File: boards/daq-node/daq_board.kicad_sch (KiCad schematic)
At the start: 14 parts, among them J1 917784-1, J11 Conn_01x19_Socket, J12 Conn_01x19_Socket, J4 917781-1, J7 917783-1

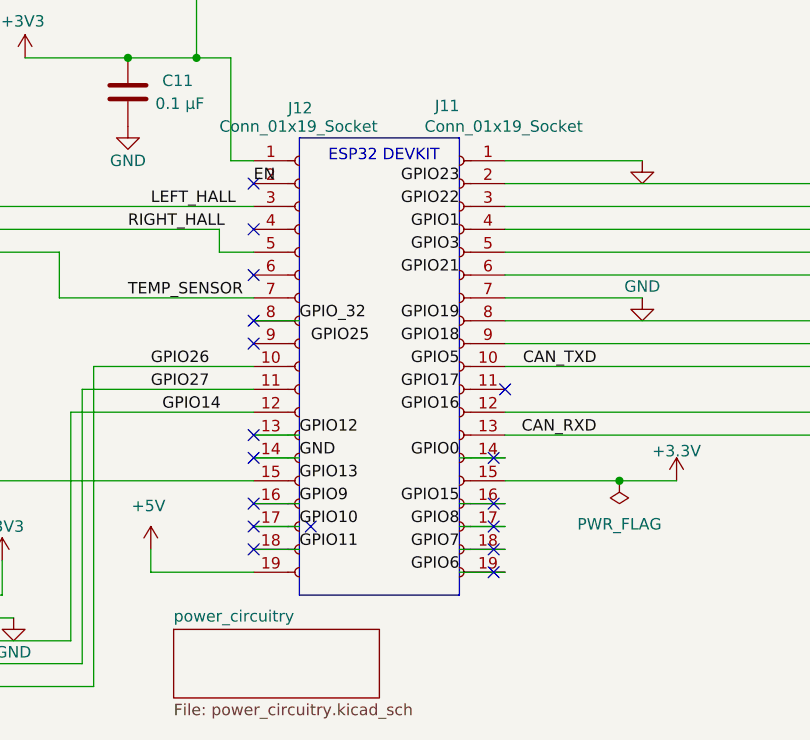
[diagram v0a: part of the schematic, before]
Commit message: Add auxiliary boards to harness; fix daq + hud ERC errors
Harness / diagram:
- Support repeated boards in the car diagram by importing one generated
  YAML under multiple include aliases; the renderer now namespaces each
  component's layout zone by its alias so instances get their own column
  (harness/wirelab/parser.py).
- Add wheel-hall (x4), fuel-sensor, and ecvt-hall aux boards as
  hand-written placeholder generated/*.yaml, instanced and wired in
  car.yaml (front wheels -> HUD J5, rear -> daq J7, eCVT halls -> ecvt J3,
  fuel -> daq J4). Documented the pattern in harness/README.md.
- extract_connectors.py now also identifies off-board connectors by
  footprint family, so a connector whose Value is left generic
  (e.g. Conn_01x04) but whose footprint is a 917xxx/Molex part is no
  longer dropped. This recovered HUD J5 (wheel power).

Board ERC fixes:
- daq-node: resolve ERC errors (dangling GPIO labels, undriven power
  pin, power-flag conflicts).
- hud-node: finish the +3.3V -> +3V3 power-symbol rename across all
  sheets (MCU sheet was missed), which had split the 3.3V net and left
  an undriven power pin on the Can sheet.

Co-Authored-By: Claude Opus 4.8 <noreply@anthropic.com>
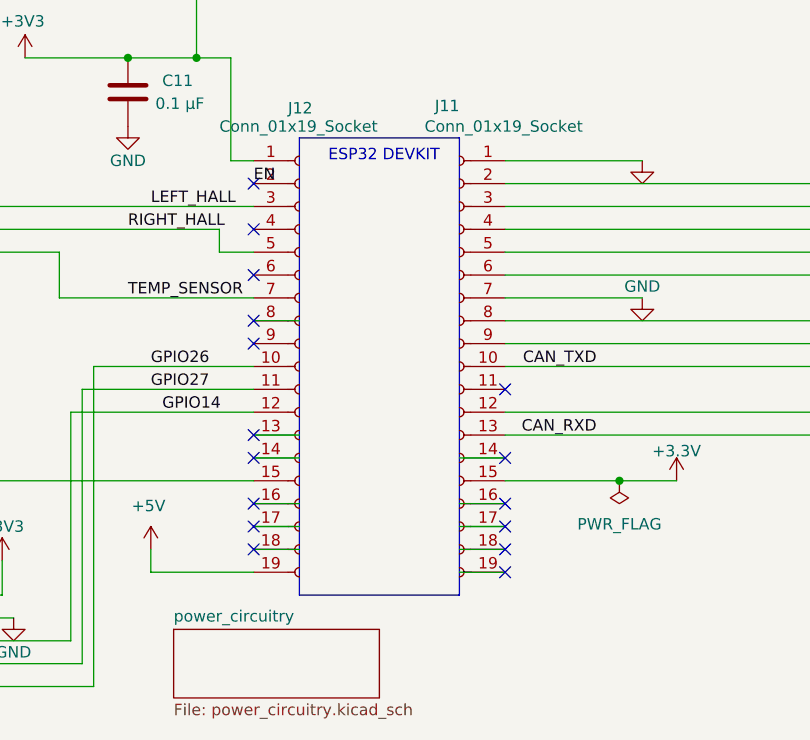
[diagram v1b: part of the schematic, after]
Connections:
- net GND: no longer J12.14 (Pin_14)
- net GPIO0: no longer names the net of J11.14 (Pin_14)
- net GPIO10: no longer names the net of J12.17 (Pin_17)
- net GPIO11: no longer names the net of J12.18 (Pin_18)
- net GPIO12: no longer names the net of J12.13 (Pin_13)
- net GPIO15: no longer names the net of J11.16 (Pin_16)
- net GPIO6: no longer names the net of J11.19 (Pin_19)
- net GPIO7: no longer names the net of J11.18 (Pin_18)
- net GPIO8: no longer names the net of J11.17 (Pin_17)
- net GPIO9: no longer names the net of J12.16 (Pin_16)
- net GPIO_32: no longer names the net of J12.8 (Pin_8)
- no-connect marks 17 -> 16
